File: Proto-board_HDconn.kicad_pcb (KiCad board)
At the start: 2 copper layers, 88.9 x 127 mm, 102 parts, among them J1 Conn_01x02, J2 Conn_01x06, J3 Conn_01x05, J4 Conn_01x05, J5 Conn_01x05, J6 Conn_01x05, J7 Conn_01x16, J9 Conn_02x06_Odd_Even, SW1 9001-XX-00, SW10 9001-XX-00, SW11 9001-XX-00, SW12 9001-XX-00, SW13 9001-XX-00, SW14 9001-XX-00, SW15 9001-XX-00, SW16 9001-XX-00, SW17 9001-XX-00, SW18 9001-XX-00, SW19 9001-XX-00, SW2 9001-XX-00, SW20 9001-XX-00, SW3 9001-XX-00, SW4 9001-XX-00, SW5 9001-XX-00, SW6 9001-XX-00, SW7 9001-XX-00, SW8 9001-XX-00, SW9 9001-XX-00, U1 TPL7407LA, U2 MAX17502, U3 XC2C128-VQ100, U4 TPL7407LA, U5 TPL7407LA, U6 MAX15027

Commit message: Final version of protoboard prior to major revision.
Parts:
- removed the REF** at (177.1, 130.6)
- removed the REF** at (174.5, 130.6)
- removed the REF** at (172.0, 130.6)
- removed the REF** at (186.7, 117.6)
- removed the REF** at (218.2, 127.8)
- removed the REF** at (182.2, 130.6)
- added REF**: PINTST, Connectors:PINTST, F.Cu at (184.7, 126.7)
- added REF**: PINTST, Connectors:PINTST, F.Cu at (250.5, 192.5)
- added REF**: PINTST, Connectors:PINTST, F.Cu at (252.0, 146.8)
- added REF**: PINTST, Connectors:PINTST, F.Cu at (230.4, 206.8)
- added REF**: PINTST, Connectors:PINTST, F.Cu at (187.2, 207.3)
- added REF**: PINTST, Connectors:PINTST, F.Cu at (198.4, 200.9)
- added REF**: PINTST, Connectors:PINTST, F.Cu at (231.2, 193.5)
- added REF**: PINTST, Connectors:PINTST, F.Cu at (214.4, 193.5)
- added REF**: PINTST, Connectors:PINTST, F.Cu at (198.2, 193.5)
- added REF**: PINTST, Connectors:PINTST, F.Cu at (178.8, 194.1)
- added REF**: PINTST, Connectors:PINTST, F.Cu at (241.6, 169.9)
- added REF**: PINTST, Connectors:PINTST, F.Cu at (192.1, 126.7)
- added REF**: PINTST, Connectors:PINTST, F.Cu at (225.1, 169.9)
- added REF**: PINTST, Connectors:PINTST, F.Cu at (175.5, 169.9)
- added REF**: PINTST, Connectors:PINTST, F.Cu at (192.1, 169.9)
- added REF**: PINTST, Connectors:PINTST, F.Cu at (208.6, 169.9)
- added REF**: PINTST, Connectors:PINTST, F.Cu at (235.5, 146.3)
- added REF**: PINTST, Connectors:PINTST, F.Cu at (220.2, 146.3)
- added REF**: PINTST, Connectors:PINTST, F.Cu at (202.5, 146.3)
- added REF**: PINTST, Connectors:PINTST, F.Cu at (187.2, 146.3)
- added REF**: PINTST, Connectors:PINTST, F.Cu at (166.9, 146.3)
- added REF**: PINTST, Connectors:PINTST, F.Cu at (198.4, 122.2)
- added REF**: PINTST, Connectors:PINTST, F.Cu at (171.2, 126.5)
- added REF**: PINTST, Connectors:PINTST, F.Cu at (187.2, 93.5)
- added REF**: PINTST, Connectors:PINTST, F.Cu at (192.3, 111.3)
- added REF**: PINTST, Connectors:PINTST, F.Cu at (238.0, 106.2)
- added REF**: PINTST, Connectors:PINTST, F.Cu at (238.0, 116.3)
- added REF**: PINTST, Connectors:PINTST, F.Cu at (238.0, 126.5)
- added REF**: PINTST, Connectors:PINTST, F.Cu at (227.9, 126.5)
- added REF**: PINTST, Connectors:PINTST, F.Cu at (229.4, 110.7)
- added REF**: PINTST, Connectors:PINTST, F.Cu at (210.6, 115.3)
- added REF**: PINTST, Connectors:PINTST, F.Cu at (215.2, 110.7)
- added REF**: PINTST, Connectors:PINTST, F.Cu at (171.2, 120.7)
- added REF**: PINTST, Connectors:PINTST, F.Cu at (206.0, 110.7)
- added REF**: PINTST, Connectors:PINTST, F.Cu at (210.6, 106.2)
- added REF**: PINTST, Connectors:PINTST, F.Cu at (179.4, 115.1)
- added REF**: PINTST, Connectors:PINTST, F.Cu at (171.2, 115.1)
- added REF**: PINTST, Connectors:PINTST, F.Cu at (171.2, 108.7)
- added REF**: PINTST, Connectors:PINTST, F.Cu at (177.3, 110.2)
- added REF**: PINTST, Connectors:PINTST, F.Cu at (250.7, 207.8)
- added TPA1: TEST, Measurement_Points:Measurement_Point_Round-TH_Small, F.Cu at (206.9, 216.7)
- added TPA2: TEST, Measurement_Points:Measurement_Point_Round-TH_Small, F.Cu at (171.9, 216.7)
- added TPB1: TEST, Measurement_Points:Measurement_Point_Round-TH_Small, F.Cu at (171.9, 214.1)
- added TPB2: TEST, Measurement_Points:Measurement_Point_Round-TH_Small, F.Cu at (206.9, 214.1)
- added TPC1: TEST, Measurement_Points:Measurement_Point_Round-TH_Small, F.Cu at (211.9, 216.7)
- added TPC2: TEST, Measurement_Points:Measurement_Point_Round-TH_Small, F.Cu at (246.9, 216.7)
- added TPD1: TEST, Measurement_Points:Measurement_Point_Round-TH_Small, F.Cu at (246.9, 214.1)
- C1, C11, C12, C13, C14, C18, C2, C3, C4, C5, C6: footprint Capacitors_SMD:C_1206_HandSoldering -> passives_IKM:1206_PROTO
- J7: footprint Pin_Headers:Pin_Header_Straight_2x08_Pitch1.00mm_SMD -> Pin_Headers:Pin_Header_Straight_2x08_Pitch2.00mm_SMD
- L1: footprint Inductors_SMD:L_Coilcraft_XAL5030 -> coilcraft_IKM:LPS6235
- R1, R2, R3, R4: footprint Resistors_SMD:R_1206_HandSoldering -> Resistors_SMD:R_0805
- U2: footprint Housings_DFN_QFN:DFN-10-1EP_3x3mm_Pitch0.5mm -> Housings_DFN_QFN:DFN-10-1EP_2x3mm_Pitch0.5mm
- moved REF** 8.70 mm to (211.4, 126.7)
- moved REF** 6.82 mm to (225.8, 118.1)
- moved C12 3.00 mm to (209.1, 124.5), turned to 315 degrees
- moved R2 1.78 mm to (169.2, 102.4)
- moved C14 1.76 mm to (213.1, 123.7), turned to 270 degrees
- moved C5 1.54 mm to (200.7, 119.9), turned to 225 degrees
- moved REF** 1.27 mm to (218.2, 126.5)
- moved R1 1.05 mm to (169.2, 98.6)
- moved C13 0.76 mm to (205.0, 136.2)
- moved C18 0.76 mm to (218.4, 136.1)
- moved C6 0.76 mm to (191.3, 136.1)
- moved C4 0.73 mm to (221.3, 103.4)
- moved C1 0.73 mm to (223.8, 109.7)
- moved C11 0.73 mm to (223.8, 115.3)
- turned L1 to 90 degrees
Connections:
- J3 pad 5: GNDREF -> GNDS
- J4 pad 5: GNDREF -> GNDS
- J5 pad 5: GNDREF -> GNDS
- J6 pad 5: GNDREF -> GNDS
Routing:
- net /TA+: track 0.00 -> 219.2 mm
- net /TB+: track 0.00 -> 205.2 mm
- net /3V3: track 89.3 -> 173.4 mm
- net GND: track 2.37 -> 50.7 mm
- net GNDREF: track 0.00 -> 29.1 mm
- net /1V8: track 89.9 -> 106.0 mm
- net /TA-: track 0.00 -> 10.9 mm
- net /TB-: track 0.00 -> 6.46 mm
- net (no net): track 0.00 -> 6.46 mm
- net /SS1.1: track 81.4 -> 75.4 mm
- net /SS4.4: track 16.7 -> 12.0 mm
- net /SS1.2: track 68.5 -> 63.9 mm
- net /SW4.1: track 39.5 -> 36.5 mm
- net /SW4.2: track 49.0 -> 46.0 mm
- net /SS2.2: track 55.3 -> 52.4 mm
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- added copper zone on F.Cu, net /TA-
- added copper zone on F.Cu, net /TB-
- added copper zone on B.Cu, net GNDS
- added copper zone on F.Cu, net GNDS
- removed copper zone on B.Cu, net /3V3
- removed copper zone on B.Cu, net GND
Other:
- board size 88.9 x 127 mm -> 88.9 x 137.2 mm
- rule trace_min: 0.1524 -> 0.152
- board text removed: "SMU"

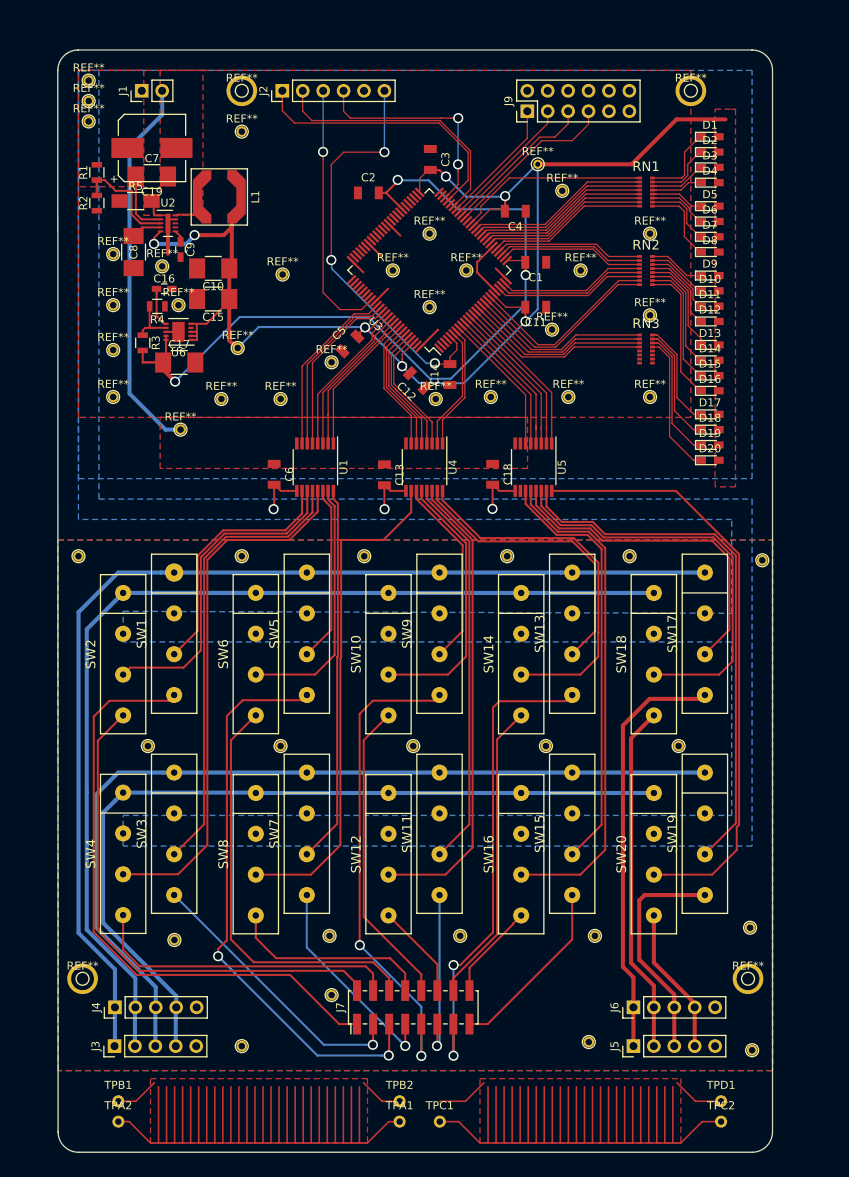
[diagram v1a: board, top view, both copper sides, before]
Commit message: Second version (4x6 card) revC, which was ordered.
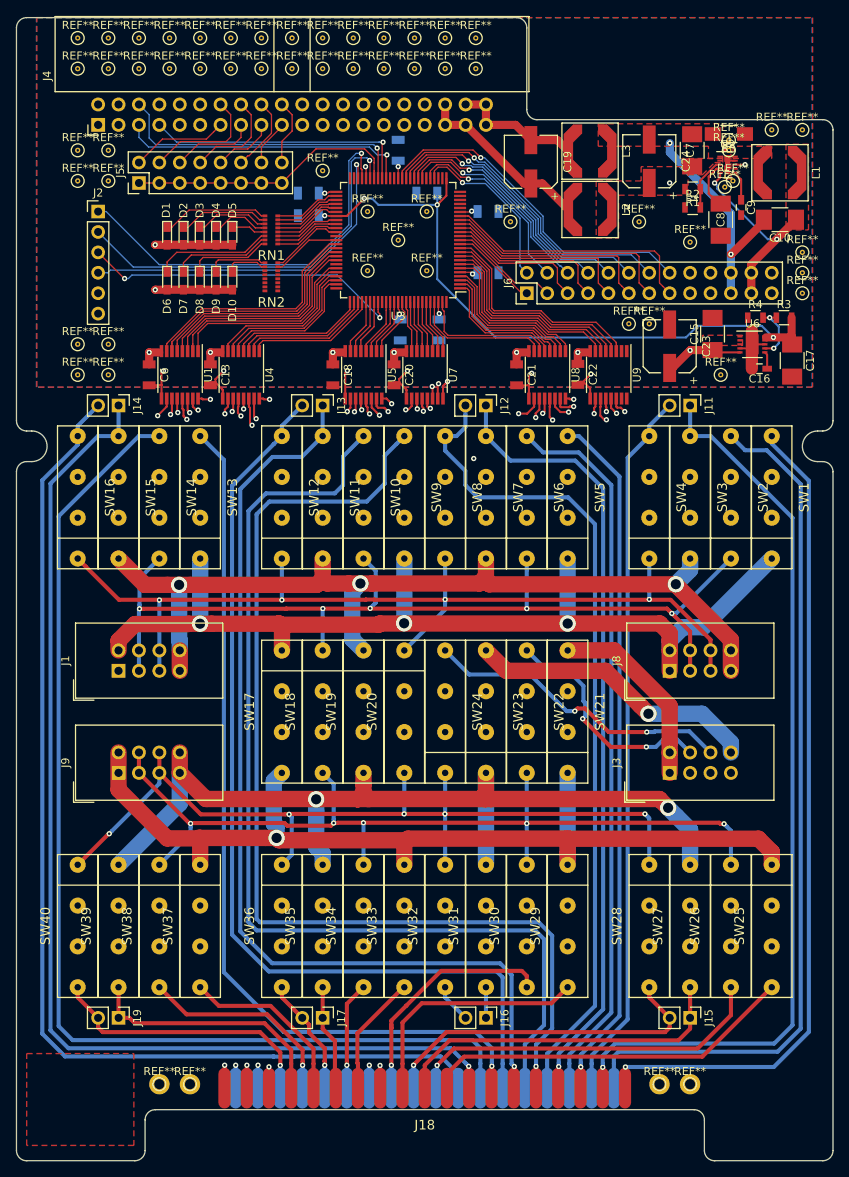
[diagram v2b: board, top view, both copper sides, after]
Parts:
- removed D11, D12, D13, D14, D15, D16, D17, D18, D19, D20: LED, LEDs:LED_0603_HandSoldering
- removed J7: Conn_01x16, Pin_Headers:Pin_Header_Straight_2x08_Pitch2.00mm_SMD
- removed the REF** at (184.7, 126.7)
- removed the REF** at (250.5, 192.5)
- removed the REF** at (252.0, 146.8)
- removed the REF** at (230.4, 206.8)
- removed the REF** at (187.2, 207.3)
- removed the REF** at (198.4, 200.9)
- removed the REF** at (231.2, 193.5)
- removed the REF** at (214.4, 193.5)
- removed the REF** at (198.2, 193.5)
- removed the REF** at (178.8, 194.1)
- removed the REF** at (241.6, 169.9)
- removed the REF** at (192.1, 126.7)
- removed the REF** at (225.1, 169.9)
- removed the REF** at (175.5, 169.9)
- removed the REF** at (192.1, 169.9)
- removed the REF** at (208.6, 169.9)
- removed the REF** at (235.5, 146.3)
- removed the REF** at (220.2, 146.3)
- removed the REF** at (202.5, 146.3)
- removed the REF** at (187.2, 146.3)
- removed the REF** at (166.9, 146.3)
- removed the REF** at (198.4, 122.2)
- removed the REF** at (171.2, 126.5)
- removed the REF** at (187.2, 93.5)
- removed the REF** at (192.3, 111.3)
- removed the REF** at (179.6, 130.6)
- removed the REF** at (238.0, 106.2)
- removed the REF** at (238.0, 116.3)
- removed the REF** at (238.0, 126.5)
- removed the REF** at (227.9, 126.5)
- removed the REF** at (229.4, 110.7)
- removed the REF** at (210.6, 115.3)
- removed the REF** at (215.2, 110.7)
- removed the REF** at (171.2, 120.7)
- removed the REF** at (206.0, 110.7)
- removed the REF** at (210.6, 106.2)
- removed the REF** at (168.2, 92.2)
- removed the REF** at (168.2, 89.7)
- removed the REF** at (168.2, 87.1)
- removed the REF** at (227.1, 100.8)
- removed the REF** at (225.8, 118.1)
- removed the REF** at (218.2, 126.5)
- removed the REF** at (211.4, 126.7)
- removed the REF** at (186.7, 120.4)
- removed the REF** at (179.4, 115.1)
- removed the REF** at (167.4, 198.9)
- removed the REF** at (250.2, 198.9)
- removed the REF** at (243.1, 88.4)
- removed the REF** at (187.2, 88.4)
- removed the REF** at (224.1, 97.5)
- removed the REF** at (171.2, 115.1)
- removed the REF** at (171.2, 108.7)
- removed the REF** at (177.3, 110.2)
- removed the REF** at (250.7, 207.8)
- removed RN3: R_Pack08, resistor_array_IKM:SOIC-16
- removed TPA1, TPA2, TPB1, TPB2, TPC1, TPC2, TPD1: TEST, Measurement_Points:Measurement_Point_Round-TH_Small
- added C20: 0.1uF, passives_IKM:1206_PROTO, F.Cu at (206.2, 123.7)
- added C21: 0.1uF, passives_IKM:1206_PROTO, F.Cu at (221.4, 123.7)
- added C22: 0.1uF, passives_IKM:1206_PROTO, F.Cu at (229.0, 123.7)
- added C23: CP, Capacitors_SMD:CP_Elec_6.3x4.5, F.Cu at (240.5, 120.2)
- added C24: CP, Capacitors_SMD:CP_Elec_6.3x4.5, F.Cu at (237.9, 97.2)
- added G***: LOGO, topi:TopiLogo, F.Cu at (166.8, 213.9)
- added J11: Conn_01x02, Pin_Headers:Pin_Header_Straight_1x02_Pitch2.54mm, F.Cu at (243.0, 127.5)
- added J12: Conn_01x02, Pin_Headers:Pin_Header_Straight_1x02_Pitch2.54mm, F.Cu at (217.6, 127.5)
- added J13: Conn_01x02, Pin_Headers:Pin_Header_Straight_1x02_Pitch2.54mm, F.Cu at (197.3, 127.5)
- added J14: Conn_01x02, Pin_Headers:Pin_Header_Straight_1x02_Pitch2.54mm, F.Cu at (171.9, 127.5)
- added J15: Conn_01x02, Pin_Headers:Pin_Header_Straight_1x02_Pitch2.54mm, F.Cu at (243.0, 203.7)
- added J16: Conn_01x02, Pin_Headers:Pin_Header_Straight_1x02_Pitch2.54mm, F.Cu at (217.6, 203.7)
- added J17: Conn_01x02, Pin_Headers:Pin_Header_Straight_1x02_Pitch2.54mm, F.Cu at (197.3, 203.7)
- added J18: DB37_Female, dsub_IKM:DC37_F_Straddle, F.Cu at (210.0, 215.2)
- added J19: Conn_01x02, Pin_Headers:Pin_Header_Straight_1x02_Pitch2.54mm, F.Cu at (171.9, 203.7)
- added J8: Conn_01x08, Connectors_IDC:IDC-Header_2x04_Pitch2.54mm_Straight, F.Cu at (240.5, 160.6)
- added L2: LPS6235-153, coilcraft_IKM:LPS6235, F.Cu at (230.6, 103.2)
- added L3: LPS6235-153, coilcraft_IKM:LPS6235, F.Cu at (230.6, 95.9)
- added REF**: PINTST, Connectors:PINTST, F.Cu at (177.0, 212.0)
- added REF**: PINTST, Connectors:PINTST, F.Cu at (197.3, 98.3)
- added REF**: PINTST, Connectors:PINTST, F.Cu at (166.8, 123.7)
- added REF**: PINTST, Connectors:PINTST, F.Cu at (170.6, 123.7)
- added REF**: PINTST, Connectors:PINTST, F.Cu at (170.6, 119.9)
- added REF**: PINTST, Connectors:PINTST, F.Cu at (166.8, 119.9)
- added REF**: PINTST, Connectors:PINTST, F.Cu at (170.6, 99.6)
- added REF**: PINTST, Connectors:PINTST, F.Cu at (166.8, 95.8)
- added REF**: PINTST, Connectors:PINTST, F.Cu at (170.6, 95.8)
- added REF**: PINTST, Connectors:PINTST, F.Cu at (166.8, 99.6)
- added REF**: PINTST, Connectors:PINTST, F.Cu at (204.9, 85.6)
- added REF**: PINTST, Connectors:PINTST, F.Cu at (180.8, 212.0)
- added REF**: PINTST, Connectors:PINTST, F.Cu at (212.5, 85.6)
- added REF**: PINTST, Connectors:PINTST, F.Cu at (216.3, 85.6)
- added REF**: PINTST, Connectors:PINTST, F.Cu at (201.1, 85.6)
- added REF**: PINTST, Connectors:PINTST, F.Cu at (208.7, 85.6)
- added REF**: PINTST, Connectors:PINTST, F.Cu at (174.4, 85.6)
- added REF**: PINTST, Connectors:PINTST, F.Cu at (178.2, 85.6)
- added REF**: PINTST, Connectors:PINTST, F.Cu at (170.6, 85.6)
- added REF**: PINTST, Connectors:PINTST, F.Cu at (182.1, 85.6)
- added REF**: PINTST, Connectors:PINTST, F.Cu at (189.7, 85.6)
- added REF**: PINTST, Connectors:PINTST, F.Cu at (166.8, 85.6)
- added REF**: PINTST, Connectors:PINTST, F.Cu at (243.0, 212.0)
- added REF**: PINTST, Connectors:PINTST, F.Cu at (185.9, 85.6)
- added REF**: PINTST, Connectors:PINTST, F.Cu at (197.3, 85.6)
- added REF**: PINTST, Connectors:PINTST, F.Cu at (193.5, 85.6)
- added REF**: PINTST, Connectors:PINTST, F.Cu at (216.3, 81.8)
- added REF**: PINTST, Connectors:PINTST, F.Cu at (212.5, 81.8)
- added REF**: PINTST, Connectors:PINTST, F.Cu at (204.9, 81.8)
- added REF**: PINTST, Connectors:PINTST, F.Cu at (201.1, 81.8)
- added REF**: PINTST, Connectors:PINTST, F.Cu at (197.3, 81.8)
- added REF**: PINTST, Connectors:PINTST, F.Cu at (193.5, 81.8)
- added REF**: PINTST, Connectors:PINTST, F.Cu at (208.7, 81.8)
- added REF**: PINTST, Connectors:PINTST, F.Cu at (239.2, 212.0)
- added REF**: PINTST, Connectors:PINTST, F.Cu at (189.7, 81.8)
- added REF**: PINTST, Connectors:PINTST, F.Cu at (185.9, 81.8)
- added REF**: PINTST, Connectors:PINTST, F.Cu at (182.1, 81.8)
- added REF**: PINTST, Connectors:PINTST, F.Cu at (178.2, 81.8)
- added REF**: PINTST, Connectors:PINTST, F.Cu at (174.4, 81.8)
- added REF**: PINTST, Connectors:PINTST, F.Cu at (170.6, 81.8)
- added REF**: PINTST, Connectors:PINTST, F.Cu at (166.8, 81.8)
- added REF**: PINTST, Connectors:PINTST, F.Cu at (220.7, 104.7)
- added REF**: PINTST, Connectors:PINTST, F.Cu at (235.4, 117.4)
- added REF**: PINTST, Connectors:PINTST, F.Cu at (237.9, 117.4)
- added REF**: PINTST, Connectors:PINTST, F.Cu at (248.3, 99.6)
- added REF**: PINTST, Connectors:PINTST, F.Cu at (257.0, 113.6)
- added REF**: PINTST, Connectors:PINTST, F.Cu at (257.0, 111.0)
- added REF**: PINTST, Connectors:PINTST, F.Cu at (257.0, 108.5)
- added REF**: PINTST, Connectors:PINTST, F.Cu at (257.0, 93.3)
- added REF**: PINTST, Connectors:PINTST, F.Cu at (253.2, 93.3)
- added REF**: PINTST, Connectors:PINTST, F.Cu at (236.7, 104.7)
- added REF**: PINTST, Connectors:PINTST, F.Cu at (243.0, 107.2)
- added REF**: PINTST, Connectors:PINTST, F.Cu at (202.9, 103.4)
- added REF**: PINTST, Connectors:PINTST, F.Cu at (210.2, 103.4)
- added REF**: PINTST, Connectors:PINTST, F.Cu at (210.2, 110.8)
- added REF**: PINTST, Connectors:PINTST, F.Cu at (247.8, 94.5)
- added REF**: PINTST, Connectors:PINTST, F.Cu at (202.9, 110.8)
- added REF**: PINTST, Connectors:PINTST, F.Cu at (206.7, 107.0)
- added REF**: PINTST, Connectors:PINTST, F.Cu at (247.8, 95.8)
- added REF**: PINTST, Connectors:PINTST, F.Cu at (247.3, 100.4)
- added REF**: PINTST, Connectors:PINTST, F.Cu at (246.8, 123.7)
- added SW21: 9001-XX-00, relay_IKM:SIP-4, F.Cu at (227.8, 165.6)
- added SW22: 9001-XX-00, relay_IKM:SIP-4, F.Cu at (222.7, 165.6)
- added SW23: 9001-XX-00, relay_IKM:SIP-4, F.Cu at (217.6, 165.6)
- added SW24: 9001-XX-00, relay_IKM:SIP-4, F.Cu at (212.5, 165.6)
- added SW25: 9001-XX-00, relay_IKM:SIP-4, F.Cu at (253.2, 192.3)
- added SW26: 9001-XX-00, relay_IKM:SIP-4, F.Cu at (248.1, 192.3)
- added SW27: 9001-XX-00, relay_IKM:SIP-4, F.Cu at (243.0, 192.3)
- added SW28: 9001-XX-00, relay_IKM:SIP-4, F.Cu at (237.9, 192.3)
- added SW29: 9001-XX-00, relay_IKM:SIP-4, F.Cu at (227.8, 192.3)
- added SW30: 9001-XX-00, relay_IKM:SIP-4, F.Cu at (222.7, 192.3)
- added SW31: 9001-XX-00, relay_IKM:SIP-4, F.Cu at (217.6, 192.3)
- added SW32: 9001-XX-00, relay_IKM:SIP-4, F.Cu at (212.5, 192.3)
- added SW33: 9001-XX-00, relay_IKM:SIP-4, F.Cu at (207.5, 192.3)
- added SW34: 9001-XX-00, relay_IKM:SIP-4, F.Cu at (202.4, 192.3)
- added SW35: 9001-XX-00, relay_IKM:SIP-4, F.Cu at (197.3, 192.3)
- added SW36: 9001-XX-00, relay_IKM:SIP-4, F.Cu at (192.2, 192.3)
- added SW37: 9001-XX-00, relay_IKM:SIP-4, F.Cu at (182.1, 192.3)
- added SW38: 9001-XX-00, relay_IKM:SIP-4, F.Cu at (177.0, 192.3)
- added SW39: 9001-XX-00, relay_IKM:SIP-4, F.Cu at (171.9, 192.3)
- added SW40: 9001-XX-00, relay_IKM:SIP-4, F.Cu at (166.8, 192.3)
- added U7: TPL7407LA, Housings_SSOP:TSSOP-16_4.4x5mm_Pitch0.65mm, F.Cu at (210.0, 123.7)
- added U8: TPL7407LA, Housings_SSOP:TSSOP-16_4.4x5mm_Pitch0.65mm, F.Cu at (225.2, 123.7)
- added U9: TPL7407LA, Housings_SSOP:TSSOP-16_4.4x5mm_Pitch0.65mm, F.Cu at (232.9, 123.7)
- C1, C11, C12, C14, C2, C3, C4, C5: moved to B.Cu
- C19: footprint Capacitors_SMD:CP_Elec_8x5.4 -> Capacitors_SMD:CP_Elec_6.3x4.5
- J1: value Conn_01x02 -> Conn_01x08; footprint Pin_Headers:Pin_Header_Straight_1x02_Pitch2.54mm -> Connectors_IDC:IDC-Header_2x04_Pitch2.54mm_Straight
- J3: value Conn_01x05 -> Conn_01x08; footprint Pin_Headers:Pin_Header_Straight_1x05_Pitch2.54mm -> Connectors_IDC:IDC-Header_2x04_Pitch2.54mm_Straight
- J4: value Conn_01x05 -> Conn_02x20_Odd_Even; footprint Pin_Headers:Pin_Header_Straight_1x05_Pitch2.54mm -> Connectors_IDC:IDC-Header_2x20_Pitch2.54mm_Angled
- J5: value Conn_01x05 -> Conn_02x08_Odd_Even; footprint Pin_Headers:Pin_Header_Straight_1x05_Pitch2.54mm -> Pin_Headers:Pin_Header_Straight_2x08_Pitch2.54mm
- J6: value Conn_01x05 -> Conn_02x13_Odd_Even; footprint Pin_Headers:Pin_Header_Straight_1x05_Pitch2.54mm -> Pin_Headers:Pin_Header_Straight_2x13_Pitch2.54mm
- J9: value Conn_02x06_Odd_Even -> Conn_01x08; footprint Pin_Headers:Pin_Header_Straight_2x06_Pitch2.54mm -> Connectors_IDC:IDC-Header_2x04_Pitch2.54mm_Straight
- U2: value MAX17502 -> MAX17502G
- moved J5 123.8 mm to (174.4, 99.9)
- moved J4 109.8 mm to (169.4, 92.6)
- moved J9 96.8 mm to (171.9, 173.3)
- moved J6 89.8 mm to (222.7, 113.6)
- moved R3 79.9 mm to (254.7, 116.6), turned to 0 degrees
- moved SW4 79.1 mm to (237.9, 139.0), turned to 90 degrees
- moved SW2 78.1 mm to (248.1, 139.0), turned to 90 degrees
- moved J3 77.0 mm to (240.5, 173.3)
- moved SW3 76.6 mm to (243.0, 139.0), turned to 90 degrees
- moved SW1 76.3 mm to (253.2, 139.0), turned to 90 degrees
- moved C17 76.3 mm to (255.7, 122.0), turned to 270 degrees
- moved C16 74.7 mm to (251.7, 123.0), turned to 180 degrees
- moved R4 74.4 mm to (251.1, 116.6), turned to 0 degrees
- moved R5 74.3 mm to (247.8, 93.8), turned to 180 degrees
- moved R1 74.2 mm to (243.3, 100.6), turned to 180 degrees
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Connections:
- C10 pad 1: /3V3 -> VCC
- C10 pad 2: GNDREF -> GND
- C14 pad 1: /VCCJTAG -> /3V3
- C19 pad 1: VCC -> /24+S
- C19 pad 2: GND -> /24-S
- C7 pad 1: VCC -> /24+
- J1 pad 1: VCC -> /CASRC
- J1 pad 2: GND -> /CASRC
- J2 pad 6: /VCCJTAG -> /3V3
- J3 pad 1: /SS_A -> /CPDSRC
- J3 pad 2: /SS_B -> /CPDSRC
- J3 pad 3: /SS_C -> /CPDSNS
- J3 pad 4: /SS_D -> /CPDSNS
- J3 pad 5: GNDS -> /APDSNS
- J4 pad 1: /SS_A -> /SDA
- J4 pad 2: /SS_B -> /SCL
- J4 pad 3: /SS_C -> GNDREF
- J4 pad 4: /SS_D -> GNDREF
- J4 pad 5: GNDS -> /SCLK0
- J5 pad 1: /SX_A -> /CS
- J5 pad 2: /SX_B -> /CS0
- J5 pad 3: /SX_C -> /CS
- J5 pad 4: /SX_D -> /CS1
- J5 pad 5: GNDS -> /CS
- J6 pad 1: /SX_A -> /HOLD0
- J6 pad 2: /SX_B -> /ENABLE0
- J6 pad 3: /SX_C -> /HOLD1
- J6 pad 4: /SX_D -> /ENABLE1
- J6 pad 5: GNDS -> /HOLD2
- J9 pad 1: /CS -> /CBSRC
- J9 pad 2: Net-(J9-Pad2) -> /CBSRC
- J9 pad 3: /MOSI -> /CBSNS
- J9 pad 4: Net-(J9-Pad4) -> /CBSNS
- J9 pad 5: /MISO -> /ABSNS
- J9 pad 6: Net-(J9-Pad6) -> /ABSNS
- J9 pad 7: /SCLK -> /ABSRC
- J9 pad 8: Net-(J9-Pad8) -> /ABSRC
- L1 pad 2: /3V3 -> VCC
- R1 pad 2: VCC -> /24+
- RN1 pad 1: /LED1.1 -> /LED2.4
- RN1 pad 10: Net-(D7-Pad1) -> Net-(D2-Pad1)
- RN1 pad 11: Net-(D6-Pad1) -> Net-(D3-Pad1)
- RN1 pad 12: Net-(D5-Pad1) -> Net-(D4-Pad1)
- RN1 pad 13: Net-(D4-Pad1) -> Net-(D5-Pad1)
- RN1 pad 14: Net-(D3-Pad1) -> Net-(D6-Pad1)
- RN1 pad 15: Net-(D2-Pad1) -> Net-(D7-Pad1)
- RN1 pad 16: Net-(D1-Pad1) -> Net-(D8-Pad1)
- RN1 pad 2: /LED1.2 -> /LED2.3
- RN1 pad 3: /LED1.3 -> /LED2.2
- RN1 pad 4: /LED1.4 -> /LED2.1
- RN1 pad 5: /LED2.1 -> /LED1.4
- RN1 pad 6: /LED2.2 -> /LED1.3
- RN1 pad 7: /LED2.3 -> /LED1.2
- RN1 pad 8: /LED2.4 -> /LED1.1
- RN1 pad 9: Net-(D8-Pad1) -> Net-(D1-Pad1)
- RN2 pad 1: /LED3.1 -> Net-(RN2-Pad1)
- RN2 pad 10: Net-(D15-Pad1) -> Net-(D10-Pad1)
- RN2 pad 15: Net-(D10-Pad1) -> Net-(RN2-Pad15)
- RN2 pad 16: Net-(D9-Pad1) -> Net-(RN2-Pad16)
- RN2 pad 2: /LED3.2 -> Net-(RN2-Pad2)
- RN2 pad 3: /LED3.3 -> Net-(RN2-Pad3)
- RN2 pad 4: /LED3.4 -> Net-(RN2-Pad4)
- RN2 pad 5: /LED4.1 -> Net-(RN2-Pad5)
- RN2 pad 6: /LED4.2 -> Net-(RN2-Pad6)
- RN2 pad 7: /LED4.3 -> /LED3.2
- RN2 pad 8: /LED4.4 -> /LED3.1
- RN2 pad 9: Net-(D16-Pad1) -> Net-(D9-Pad1)
- SW1 pad 1: /SS_A -> /CASRC
- SW1 pad 3: /SW1.1 -> /SW1
- SW1 pad 4: /SS1.1 -> /C1ASRC
- SW10 pad 1: /SS_B -> /CASNS
- SW10 pad 3: /SW3.2 -> /SW10
- SW10 pad 4: /SS3.2 -> /C3ASNS
- SW11 pad 1: /SS_C -> /AASRC
- SW11 pad 3: /SW3.3 -> /SW11
- SW11 pad 4: /SS3.3 -> /A3ASRC
- SW12 pad 1: /SS_D -> /AASNS
- SW12 pad 3: /SW3.4 -> /SW12
- SW12 pad 4: /SS3.4 -> /A3ASNS
- SW13 pad 1: /SS_A -> /CASRC
- SW13 pad 3: /SW4.1 -> /SW13
- SW13 pad 4: /SS4.1 -> /C4ASRC
- SW14 pad 1: /SS_B -> /CASNS
- SW14 pad 3: /SW4.2 -> /SW14
- SW14 pad 4: /SS4.2 -> /C4ASNS
- SW15 pad 1: /SS_C -> /AASRC
- SW15 pad 3: /SW4.3 -> /SW15
- SW15 pad 4: /SS4.3 -> /A4ASRC
- SW16 pad 1: /SS_D -> /AASNS
- SW16 pad 3: /SW4.4 -> /SW16
- SW16 pad 4: /SS4.4 -> /A4ASNS
- SW17 pad 1: /SS_A -> /CASRC
- SW17 pad 3: /SW5.1 -> /SW17
- SW17 pad 4: /SX_A -> /CBSRC
- SW18 pad 1: /SS_B -> /CASNS
- SW18 pad 3: /SW5.2 -> /SW18
- SW18 pad 4: /SX_B -> /CBSNS
- SW19 pad 1: /SS_C -> /AASRC
- SW19 pad 3: /SW5.3 -> /SW19
- SW19 pad 4: /SX_C -> /ABSRC
- SW2 pad 1: /SS_B -> /CASNS
- SW2 pad 3: /SW1.2 -> /SW2
- SW2 pad 4: /SS1.2 -> /C1ASNS
- SW20 pad 1: /SS_D -> /AASNS
- SW20 pad 3: /SW5.4 -> /SW20
- SW20 pad 4: /SX_D -> /ABSNS
- SW3 pad 1: /SS_C -> /AASRC
- SW3 pad 3: /SW1.3 -> /SW3
- SW3 pad 4: /SS1.3 -> /A1ASRC
- SW4 pad 1: /SS_D -> /AASNS
- SW4 pad 3: /SW1.4 -> /SW4
- SW4 pad 4: /SS1.4 -> /A1ASNS
- SW5 pad 1: /SS_A -> /CASRC
- SW5 pad 3: /SW2.1 -> /SW5
- SW5 pad 4: /SS2.1 -> /C2ASRC
- SW6 pad 1: /SS_B -> /CASNS
- SW6 pad 3: /SW2.2 -> /SW6
- SW6 pad 4: /SS2.2 -> /C2ASNS
- SW7 pad 1: /SS_C -> /AASRC
- SW7 pad 3: /SW2.3 -> /SW7
- SW7 pad 4: /SS2.3 -> /A2ASRC
- SW8 pad 1: /SS_D -> /AASNS
- SW8 pad 3: /SW2.4 -> /SW8
- SW8 pad 4: /SS2.4 -> /A2ASNS
- SW9 pad 1: /SS_A -> /CASRC
- SW9 pad 3: /SW3.1 -> /SW9
- SW9 pad 4: /SS3.1 -> /C3ASRC
- U1 pad 1: /CTRL2.3 -> /CTRL38
- U1 pad 10: /SW1.1 -> /SW16
- U1 pad 11: /SW1.2 -> /SW40
- U1 pad 12: /SW1.3 -> /SW15
- U1 pad 13: /SW1.4 -> /SW39
- U1 pad 14: /SW2.1 -> /SW14
- U1 pad 15: /SW2.2 -> /SW13
- U1 pad 16: /SW2.3 -> /SW38
- U1 pad 2: /CTRL2.2 -> /CTRL13
- U1 pad 3: /CTRL2.1 -> /CTRL14
- U1 pad 4: /CTRL1.4 -> /CTRL39
- U1 pad 5: /CTRL1.3 -> /CTRL15
- U1 pad 6: /CTRL1.2 -> /CTRL40
- U1 pad 7: /CTRL1.1 -> /CTRL16
- U2 pad 2: VCC -> /24+
- U2 pad 5: /3V3 -> VCC
- U2 pad 8: Net-(U2-Pad8) -> /vccgood
- U3 pad 1: Net-(U3-Pad1) -> /CTRL21
- U3 pad 10: /CTRL5.1 -> /CTRL2
- U3 pad 11: /CTRL5.2 -> /CTRL1
- U3 pad 12: /CTRL5.3 -> /HOLD0
- U3 pad 13: /CTRL5.4 -> /HOLD1
- U3 pad 14: /LED5.4 -> /HOLD2
- U3 pad 15: /LED5.3 -> /HOLD3
- U3 pad 16: /LED5.2 -> /HOLD4
- U3 pad 17: /LED5.1 -> /HOLD5
- U3 pad 18: /LED4.4 -> /HOLD6
- U3 pad 19: /LED4.3 -> /HOLD7
- U3 pad 2: Net-(U3-Pad2) -> /CTRL5
- U3 pad 22: /LED4.2 -> Net-(U3-Pad22)
- U3 pad 23: /LED4.1 -> Net-(U3-Pad23)
- U3 pad 24: /LED3.4 -> Net-(U3-Pad24)
- U3 pad 27: /LED3.3 -> Net-(U3-Pad27)
- U3 pad 28: /LED3.2 -> Net-(U3-Pad28)
- U3 pad 29: /LED3.1 -> /ENABLE0
- U3 pad 3: Net-(U3-Pad3) -> /CTRL28
- U3 pad 30: /LED2.4 -> /ENABLE1
- U3 pad 32: /LED2.3 -> /ENABLE2
- U3 pad 33: /LED2.2 -> /ENABLE3
- U3 pad 34: /LED2.1 -> /ENABLE4
- U3 pad 35: /LED1.4 -> /ENABLE5
- U3 pad 36: /LED1.3 -> /ENABLE6
- U3 pad 37: /LED1.2 -> /ENABLE7
- U3 pad 39: /LED1.1 -> Net-(U3-Pad39)
- U3 pad 4: Net-(U3-Pad4) -> /CTRL27
- U3 pad 41: /SCLK -> /SCLK0
- U3 pad 42: /MISO -> /MISO0
- U3 pad 43: /MOSI -> /MOSI0
- U3 pad 46: Net-(U3-Pad46) -> /vccgood
- U3 pad 5: /VCCJTAG -> /3V3
- U3 pad 52: Net-(U3-Pad52) -> /LED1.1
- U3 pad 53: Net-(U3-Pad53) -> /LED1.2
- U3 pad 54: Net-(U3-Pad54) -> /LED1.3
- U3 pad 55: Net-(U3-Pad55) -> /LED1.4
- U3 pad 56: Net-(U3-Pad56) -> /LED2.1
- U3 pad 58: Net-(U3-Pad58) -> /LED2.2
- U3 pad 59: Net-(U3-Pad59) -> /LED2.3
- U3 pad 6: /CTRL4.1 -> /CTRL26
- U3 pad 60: Net-(U3-Pad60) -> /LED2.4
- U3 pad 61: Net-(U3-Pad61) -> /LED3.1
- U3 pad 63: Net-(U3-Pad63) -> /LED3.2
- U3 pad 64: Net-(U3-Pad64) -> /CTRL16
- U3 pad 65: Net-(U3-Pad65) -> /CTRL40
- U3 pad 66: Net-(U3-Pad66) -> /CTRL15
- U3 pad 67: Net-(U3-Pad67) -> /CTRL39
- U3 pad 68: Net-(U3-Pad68) -> /CTRL14
- U3 pad 7: /CTRL4.2 -> /CTRL25
- U3 pad 70: Net-(U3-Pad70) -> /CTRL13
- U3 pad 71: Net-(U3-Pad71) -> /CTRL38
- U3 pad 72: Net-(U3-Pad72) -> /CTRL37
- U3 pad 73: Net-(U3-Pad73) -> /CTRL36
- U3 pad 74: Net-(U3-Pad74) -> /CTRL17
- U3 pad 76: Net-(U3-Pad76) -> /CTRL12
- U3 pad 77: Net-(U3-Pad77) -> /CTRL35
- U3 pad 78: Net-(U3-Pad78) -> /CTRL18
- U3 pad 79: Net-(U3-Pad79) -> /CTRL11
- U3 pad 8: /CTRL4.3 -> /CTRL4
- U3 pad 80: Net-(U3-Pad80) -> /CTRL34
- U3 pad 81: Net-(U3-Pad81) -> /CTRL19
- U3 pad 82: Net-(U3-Pad82) -> /CTRL10
- U3 pad 85: /CTRL1.1 -> /CTRL33
- U3 pad 86: /CTRL1.2 -> /CTRL20
- U3 pad 87: /CTRL1.3 -> /CTRL9
- U3 pad 89: /CTRL1.4 -> /CTRL32
- U3 pad 9: /CTRL4.4 -> /CTRL3
- U3 pad 90: /CTRL2.1 -> /CTRL24
- U3 pad 91: /CTRL2.2 -> /CTRL8
- U3 pad 92: /CTRL2.3 -> /CTRL31
- U3 pad 93: /CTRL2.4 -> /CTRL23
- U3 pad 94: /CTRL3.1 -> /CTRL7
- U3 pad 95: /CTRL3.2 -> /CTRL30
- U3 pad 96: /CTRL3.3 -> /CTRL22
- U3 pad 97: /CTRL3.4 -> /CTRL6
- U3 pad 99: Net-(U3-Pad99) -> /CTRL29
- U4 pad 1: /CTRL4.2 -> /CTRL11
- U4 pad 10: /SW2.4 -> /SW37
- U4 pad 11: /SW3.1 -> /SW36
- U4 pad 12: /SW3.2 -> /SW17
- U4 pad 13: /SW3.3 -> /SW12
- U4 pad 14: /SW3.4 -> /SW35
- U4 pad 15: /SW4.1 -> /SW18
- U4 pad 16: /SW4.2 -> /SW11
- U4 pad 2: /CTRL4.1 -> /CTRL18
- U4 pad 3: /CTRL3.4 -> /CTRL35
- U4 pad 4: /CTRL3.3 -> /CTRL12
- U4 pad 5: /CTRL3.2 -> /CTRL17
- U4 pad 6: /CTRL3.1 -> /CTRL36
- U4 pad 7: /CTRL2.4 -> /CTRL37
- U5 pad 1: /CTRL5.4 -> /CTRL32
- U5 pad 10: Net-(U5-Pad10) -> /SW34
- U5 pad 11: /SW4.3 -> /SW19
- U5 pad 12: /SW4.4 -> /SW10
- U5 pad 13: /SW5.1 -> /SW33
- U5 pad 14: /SW5.2 -> /SW20
- U5 pad 15: /SW5.3 -> /SW9
- U5 pad 16: /SW5.4 -> /SW32
- U5 pad 2: /CTRL5.3 -> /CTRL9
- U5 pad 3: /CTRL5.2 -> /CTRL20
- U5 pad 4: /CTRL5.1 -> /CTRL33
- U5 pad 5: /CTRL4.4 -> /CTRL10
- U5 pad 6: /CTRL4.3 -> /CTRL19
- U5 pad 7: Net-(U5-Pad7) -> /CTRL34
- U6 pad 4: Net-(U6-Pad4) -> GNDREF
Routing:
- net VCC: track 26.5 -> 457.7 mm, vias 3 -> 8
- net /TA+: track 219.2 -> 0.00 mm
- net /TB+: track 205.2 -> 0.00 mm
- net /A4ASRC: track 0.00 -> 139.4 mm, vias 0 -> 1
- net /C4ASNS: track 0.00 -> 138.7 mm
- net /A4ASNS: track 0.00 -> 136.7 mm
- net /SS_A: track 135.9 -> 0.00 mm
- net /C3ASRC: track 0.00 -> 132.2 mm, vias 0 -> 1
- net /APDSNS: track 0.00 -> 131.0 mm, vias 0 -> 3
- net /C3ASNS: track 0.00 -> 128.6 mm
- net /APDSRC: track 0.00 -> 128.5 mm, vias 0 -> 2
- net /SS_B: track 126.8 -> 0.00 mm
- net /A3ASRC: track 0.00 -> 122.1 mm, vias 0 -> 1
- net /CASRC: track 0.00 -> 121.9 mm, vias 0 -> 3
- net /CBSRC: track 0.00 -> 120.6 mm, vias 0 -> 1
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- added copper zone on F.Cu, net (none)
- added copper zone on F.Cu, net /24+
- added copper zone on In2.Cu, net /3V3
- added copper zone on In1.Cu, net GNDREF
- added copper zone on In1.Cu, net GNDS
- added copper zone on In2.Cu, net GNDS
- added copper zone on F.Cu, net Net-(L1-Pad1)
- removed copper zone on F.Cu, net /TA-
- removed copper zone on F.Cu, net /TB-
- removed copper zone on B.Cu, net GNDS
- removed copper zone on F.Cu, net GNDS
- removed copper zone on B.Cu, net VCC
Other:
- board size 88.9 x 137.2 mm -> 101.6 x 142.2 mm
- copper layers 2 -> 4
- net class DIGITAL SIGNAL added: clearance 0.1524, trace_width 0.1524, via_dia 0.6604, via_drill 0.3048
- net class Default: via_dia 1.27 -> 0.6604; via_drill 0.889 -> 0.3048
- net class POWER: clearance 0.1524 -> 0.2032; via_dia 1.27 -> 0.6604; via_drill 0.889 -> 0.3048
- net class SIGNAL BUS added: clearance 0.508, trace_width 2.032, via_dia 2.032, via_drill 1.27
- net class SS2 removed
- net class SWITCHING SIGNAL: via_dia 1.27 -> 0.6604; via_drill 0.889 -> 0.3048
- rule trace_min: 0.152 -> 0.1524
- rule via_min_drill: 0.3 -> 0.3048
- rule via_min_size: 0.4 -> 0.6604
- board text added: "GNDS (SIGNAL) GND (POWER) GNDREF (DIGITAL)"
- board text added: "INTRODUCE HEARTBEAT INTO INTERFACE"
- board text added: "Mu-metal shield may be required if magnetic fields disrupt signals durring switching. This would also occur if a second board was used and placed closely."
- board text added: "RELAY CHANNELS CARRY 0.5AMP OF CURRENT"
- board text added: "SMU CHANNELS CARRY UP TO 3-5AMP OF CURRENT, +/- 20V"
- board text added: "SURROUND SENSITIVE PINS WITH GROUND TO PROTECT FROM VOLTAGES"
- board text removed: "CAL"

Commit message: First commit to shared repo after board fab and bring-up of 10 boards.
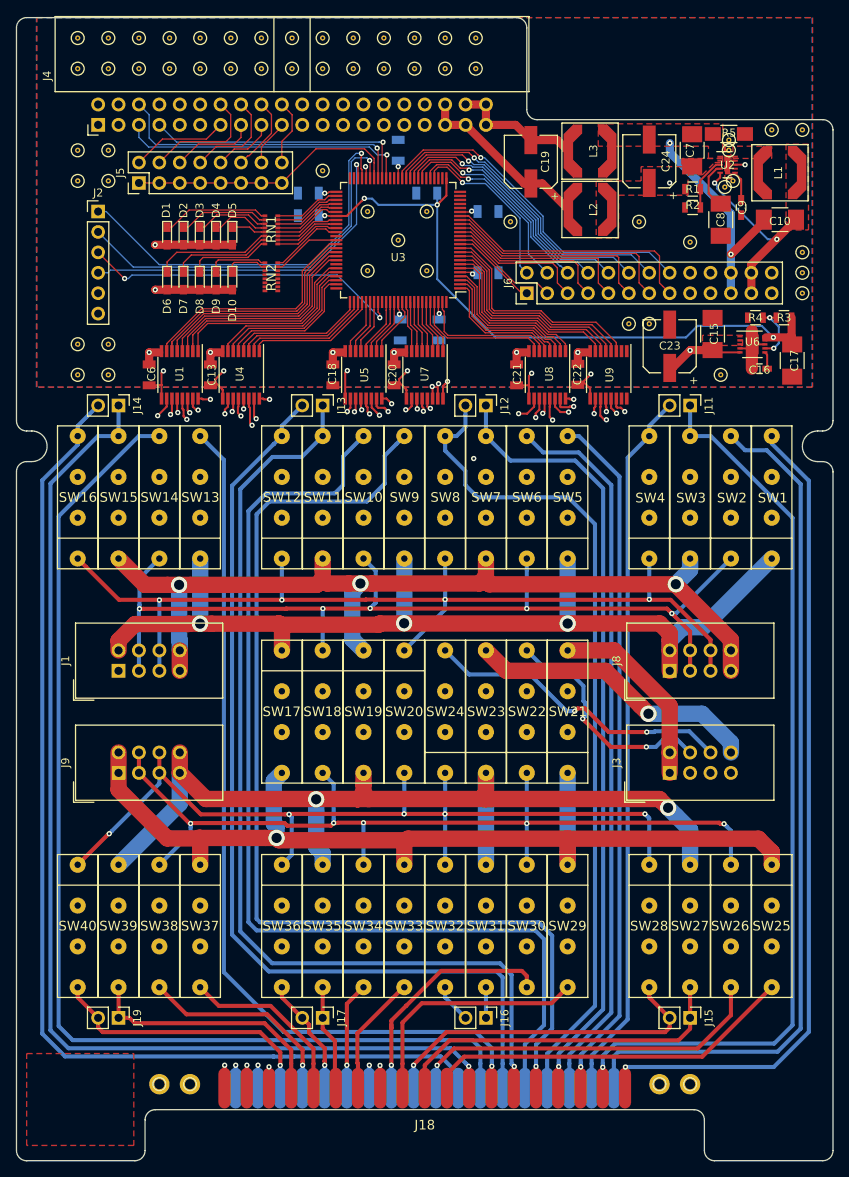
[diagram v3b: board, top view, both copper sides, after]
